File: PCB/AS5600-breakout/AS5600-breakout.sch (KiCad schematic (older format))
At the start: 1 part, among them U1 AS5600

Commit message: initial PCB for encoder
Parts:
- added C1: 100nF, Capacitor_THT:CP_Radial_D6.3mm_P2.50mm, symbol pspice:CAP
- added C2: 1uF, Capacitor_THT:CP_Radial_D8.0mm_P3.50mm, symbol pspice:CAP
- added J1, J2: Conn_01x02, Connector_PinHeader_2.54mm:PinHeader_1x02_P2.54mm_Vertical, symbol Connector_Generic:Conn_01x02
- added J3: Conn_01x05_Female, Connector_PinHeader_2.54mm:PinHeader_1x05_P2.54mm_Horizontal, symbol Connector:Conn_01x05_Female
- added J4: Conn_01x03_Male, Connector_PinHeader_2.54mm:PinHeader_1x03_P2.54mm_Vertical, symbol Connector:Conn_01x03_Male
- added R1, R2: 4.7k, Resistor_THT:R_Axial_DIN0207_L6.3mm_D2.5mm_P7.62mm_Horizontal, symbol Device:R
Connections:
- net +5V: now reaches U1.1 (VDD_5V)
- net +5V: now also C1.1, J2.2 (Pin_2), J3.1 (Pin_1), J4.3 (Pin_3), R1.1, R2.1
- net at U1.2 (VDD_3V): now also C2.1, J2.1 (Pin_1)
- net OUT: now reaches U1.3 (OUT)
- net OUT: now also J3.4 (Pin_4)
- net GND: now reaches U1.4 (GND)
- net GND: now also C1.2, C2.2, J1.2 (Pin_2), J3.5 (Pin_5), J4.1 (Pin_1)
- net at U1.5 (PGO): now also J1.1 (Pin_1)
- net SDA: now reaches U1.6 (SDA)
- net SDA: now also J3.2 (Pin_2), R2.2
- net SCL: now reaches U1.7 (SCL)
- net SCL: now also J3.3 (Pin_3), R1.2
- net DIR: now reaches U1.8 (DIR)
- net DIR: now also J4.2 (Pin_2)

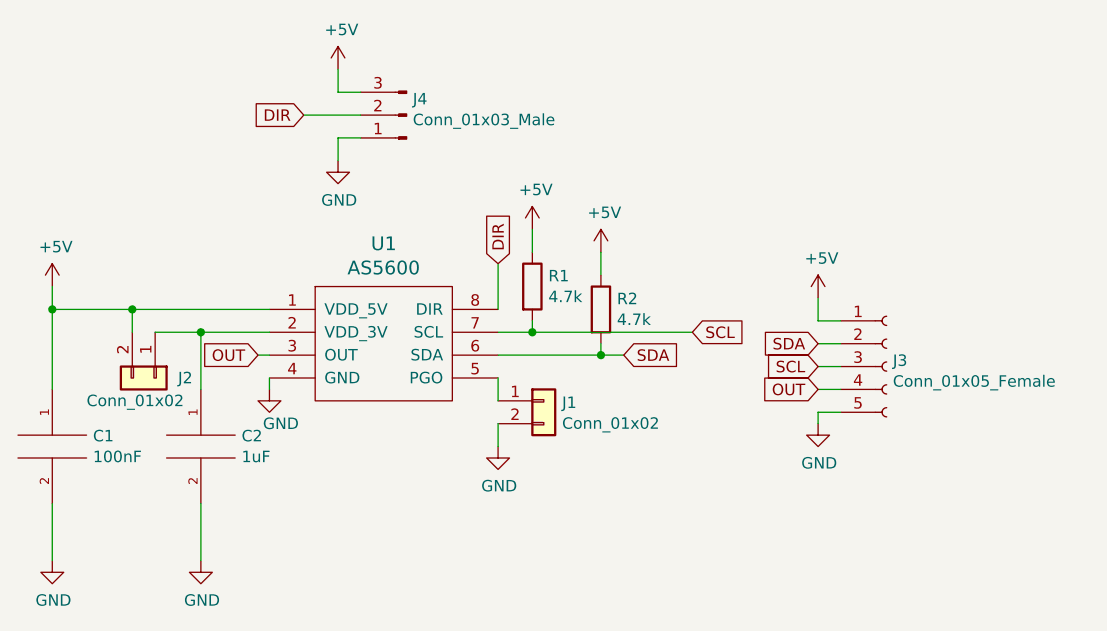
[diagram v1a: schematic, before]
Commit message: first pcb has been cut for encoders, looks good!
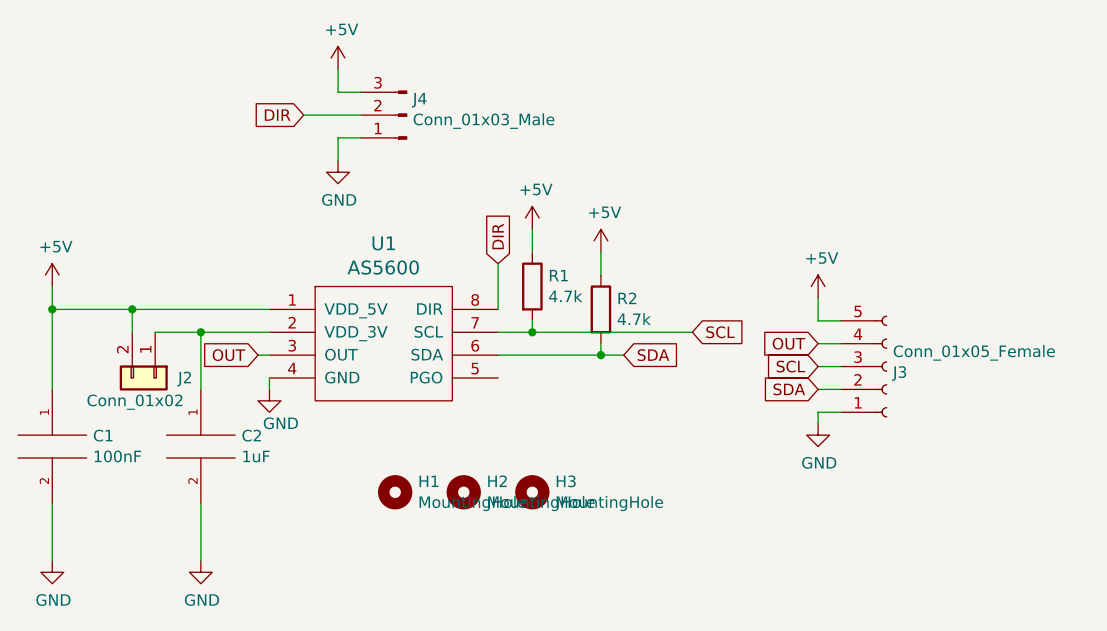
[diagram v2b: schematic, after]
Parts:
- removed J1: Conn_01x02, Connector_PinHeader_2.54mm:PinHeader_1x02_P2.54mm_Vertical, symbol Connector_Generic:Conn_01x02
- added H1, H2, H3: MountingHole, AS5600-breakout:MountingHole_2.2mm_M2_small, symbol Mechanical:MountingHole
- C1: footprint Capacitor_THT:CP_Radial_D6.3mm_P2.50mm -> Capacitor_THT:C_Disc_D4.7mm_W2.5mm_P5.00mm
- C2: footprint Capacitor_THT:CP_Radial_D8.0mm_P3.50mm -> Capacitor_THT:CP_Radial_D5.0mm_P2.00mm
- J3: footprint Connector_PinHeader_2.54mm:PinHeader_1x05_P2.54mm_Horizontal -> Connector_Molex:Molex_KK-254_AE-6410-05A_1x05_P2.54mm_Vertical
- J4: footprint Connector_PinHeader_2.54mm:PinHeader_1x03_P2.54mm_Vertical -> AS5600-breakout:SOIC127_solder_switch
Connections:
- net +5V: now also J3.5 (Pin_5); no longer J3.1 (Pin_1)
- net GND: now also J3.1 (Pin_1); no longer J3.5 (Pin_5)
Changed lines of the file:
@@
 EESchema Schematic File Version 4
 LIBS:AS5600-breakout-cache
-EELAYER 26 0
+EELAYER 29 0
 EELAYER END
 $Descr A4 11693 8268
@@
 F 0 "C1" H 3428 2896 50  0000 L CNN
 F 1 "100nF" H 3428 2805 50  0000 L CNN
-F 2 "Capacitor_THT:CP_Radial_D6.3mm_P2.50mm" H 3250 2850 50  0001 C CNN
+F 2 "Capacitor_THT:C_Disc_D4.7mm_W2.5mm_P5.00mm" H 3250 2850 50  0001 C CNN
 F 3 "~" H 3250 2850 50  0001 C CNN
 	1    3250 2850
@@
 F 0 "C2" H 4078 2896 50  0000 L CNN
 F 1 "1uF" H 4078 2805 50  0000 L CNN
-F 2 "Capacitor_THT:CP_Radial_D8.0mm_P3.50mm" H 3900 2850 50  0001 C CNN
+F 2 "Capacitor_THT:CP_Radial_D5.0mm_P2.00mm" H 3900 2850 50  0001 C CNN
 F 3 "~" H 3900 2850 50  0001 C CNN
 	1    3900 2850
@@
 	1    0    0    -1
 $EndComp
-$Comp
-L power:GND #PWR0104
-U 1 1 5CF77EB2
-P 5200 2850
-F 0 "#PWR0104" H 5200 2600 50  0001 C CNN
-F 1 "GND" H 5205 2677 50  0000 C CNN
-F 2 "" H 5200 2850 50  0001 C CNN
-F 3 "" H 5200 2850 50  0001 C CNN
-	1    5200 2850
-	1    0    0    -1
-$EndComp
 Wire Wire Line
 	5350 2300 5350 2350
@@
 Wire Wire Line
 	5650 2450 5650 2400
-$Comp
-L Connector_Generic:Conn_01x02 J1
-U 1 1 5CF78367
-P 5400 2650
-F 0 "J1" H 5480 2642 50  0000 L CNN
-F 1 "Conn_01x02" H 5480 2551 50  0000 L CNN
-F 2 "Connector_PinHeader_2.54mm:PinHeader_1x02_P2.54mm_Vertical" H 5400 2650 50  0001 C CNN
-F 3 "~" H 5400 2650 50  0001 C CNN
-	1    5400 2650
-	1    0    0    -1
-$EndComp
-Wire Wire Line
-	5200 2550 5200 2650
-Wire Wire Line
-	5200 2750 5200 2850
-$Comp
-L Connector:Conn_01x05_Female J3
-U 1 1 5CF784F9
-P 6900 2500
-F 0 "J3" H 6927 2526 50  0000 L CNN
-F 1 "Conn_01x05_Female" H 6927 2435 50  0000 L CNN
-F 2 "Connector_PinHeader_2.54mm:PinHeader_1x05_P2.54mm_Horizontal" H 6900 2500 50  0001 C CNN
-F 3 "~" H 6900 2500 50  0001 C CNN
-	1    6900 2500
-	1    0    0    -1
-$EndComp
 Text GLabel 5750 2450 2    50   Input ~ 0
 SDA
@@
 F 0 "J4" H 4773 1330 50  0000 R CNN
 F 1 "Conn_01x03_Male" H 4773 1421 50  0000 R CNN
-F 2 "Connector_PinHeader_2.54mm:PinHeader_1x03_P2.54mm_Vertical" H 4800 1400 50  0001 C CNN
+F 2 "AS5600-breakout:SOIC127_solder_switch" H 4800 1400 50  0001 C CNN
 F 3 "~" H 4800 1400 50  0001 C CNN
 	1    4800 1400
@@
 $EndComp
 Wire Wire Line
-	6700 2300 6600 2300
-Wire Wire Line
 	6600 2300 6600 2200
-Text GLabel 6600 2400 0    50   Input ~ 0
+Text GLabel 6600 2600 0    50   Input ~ 0
 SDA
 Text GLabel 6600 2500 0    50   Input ~ 0
 SCL
 Wire Wire Line
-	6700 2400 6600 2400
-Wire Wire Line
-	6700 2500 6600 2500
-$Comp
-L power:GND #PWR0110
-U 1 1 5CF7A497
-P 6600 2750
-F 0 "#PWR0110" H 6600 2500 50  0001 C CNN
-F 1 "GND" H 6605 2577 50  0000 C CNN
-F 2 "" H 6600 2750 50  0001 C CNN
-F 3 "" H 6600 2750 50  0001 C CNN
-	1    6600 2750
-	1    0    0    -1
-$EndComp
-Wire Wire Line
-	6700 2700 6600 2700
-Wire Wire Line
 	6600 2700 6600 2750
-Text GLabel 6600 2600 0    50   Input ~ 0
+Text GLabel 6600 2400 0    50   Input ~ 0
 OUT
-Wire Wire Line
-	6700 2600 6600 2600
 $Comp
 L power:+5V #PWR0111
@@
 Wire Wire Line
 	3600 2250 4200 2250
+$Comp
+L Connector:Conn_01x05_Female J3
+U 1 1 5CF784F9
+P 6900 2500
+F 0 "J3" H 6927 2526 50  0000 L CNN
+F 1 "Conn_01x05_Female" H 6927 2435 50  0000 L CNN
+F 2 "Connector_Molex:Molex_KK-254_AE-6410-05A_1x05_P2.54mm_Vertical" H 6900 2500 50  0001 C CNN
+F 3 "~" H 6900 2500 50  0001 C CNN
+	1    6900 2500
+	1    0    0    1
+$EndComp
+Wire Wire Line
+	6700 2300 6600 2300
+Wire Wire Line
+	6700 2600 6600 2600
+Wire Wire Line
+	6600 2700 6700 2700
+$Comp
+L power:GND #PWR0104
+U 1 1 5CFD15D0
+P 6600 2750
+F 0 "#PWR0104" H 6600 2500 50  0001 C CNN
+F 1 "GND" H 6605 2577 50  0000 C CNN
+F 2 "" H 6600 2750 50  0001 C CNN
+F 3 "" H 6600 2750 50  0001 C CNN
+	1    6600 2750
+	1    0    0    -1
+$EndComp
+Wire Wire Line
+	6700 2400 6600 2400
+Wire Wire Line
+	6600 2500 6700 2500
+$Comp
+L Mechanical:MountingHole H1
+U 1 1 5CFDB7FC
+P 4750 3050
+F 0 "H1" H 4850 3096 50  0000 L CNN
+F 1 "MountingHole" H 4850 3005 50  0000 L CNN
+F 2 "AS5600-breakout:MountingHole_2.2mm_M2_small" H 4750 3050 50  0001 C CNN
+F 3 "~" H 4750 3050 50  0001 C CNN
+	1    4750 3050
+	1    0    0    -1
+$EndComp
+$Comp
+L Mechanical:MountingHole H2
+U 1 1 5CFDC0C0
+P 5050 3050
+F 0 "H2" H 5150 3096 50  0000 L CNN
+F 1 "MountingHole" H 5150 3005 50  0000 L CNN
+F 2 "AS5600-breakout:MountingHole_2.2mm_M2_small" H 5050 3050 50  0001 C CNN
+F 3 "~" H 5050 3050 50  0001 C CNN
+	1    5050 3050
+	1    0    0    -1
+$EndComp
+$Comp
+L Mechanical:MountingHole H3
+U 1 1 5CFDC689
+P 5350 3050
+F 0 "H3" H 5450 3096 50  0000 L CNN
+F 1 "MountingHole" H 5450 3005 50  0000 L CNN
+F 2 "AS5600-breakout:MountingHole_2.2mm_M2_small" H 5350 3050 50  0001 C CNN
+F 3 "~" H 5350 3050 50  0001 C CNN
+	1    5350 3050
+	1    0    0    -1
+$EndComp
 $EndSCHEMATC
